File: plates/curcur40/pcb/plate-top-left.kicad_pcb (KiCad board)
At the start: 2 copper layers, 116.1 x 88.3 mm, 0 parts

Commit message: fix all
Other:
- board size 116.1 x 88.3 mm -> 125.1 x 92.6 mm
- rule pad_to_mask_clearance: 0.2 -> 0

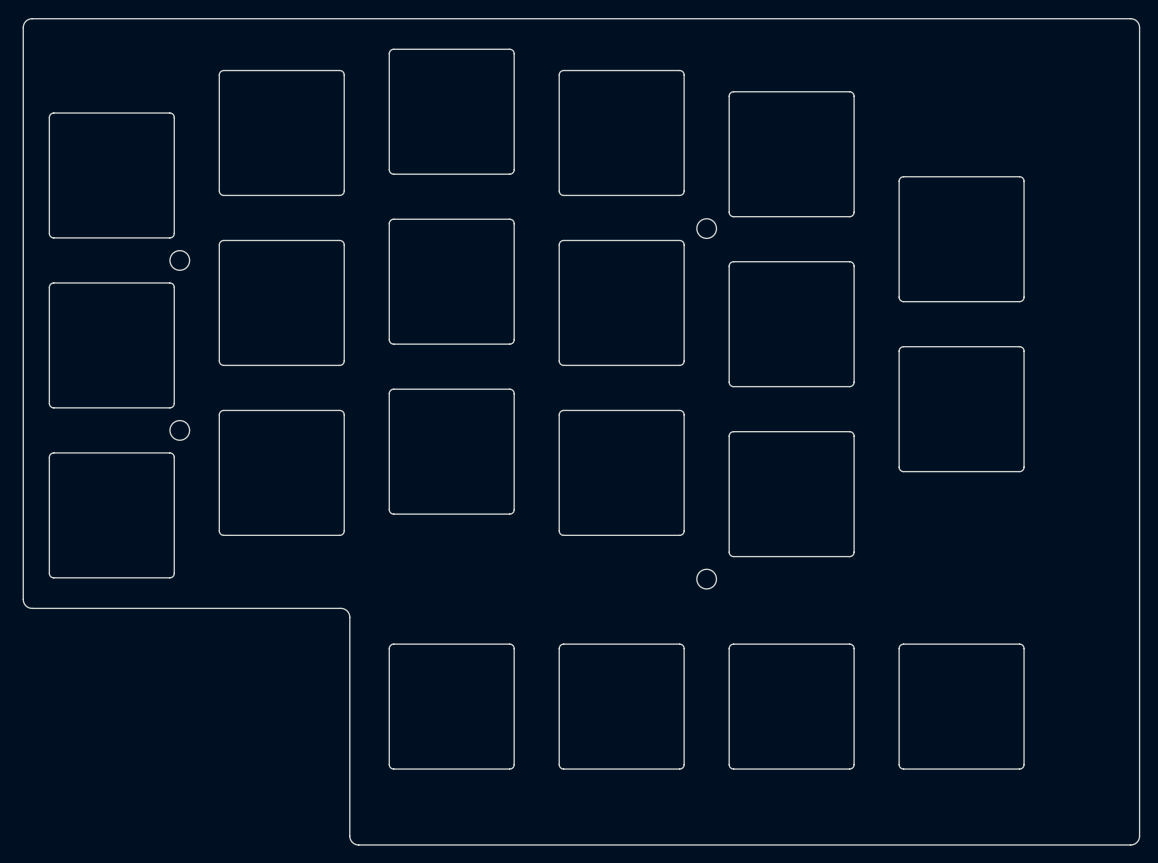
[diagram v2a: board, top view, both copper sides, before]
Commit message: Restore TRRS cutouts and relocate mounting holes to perimeter
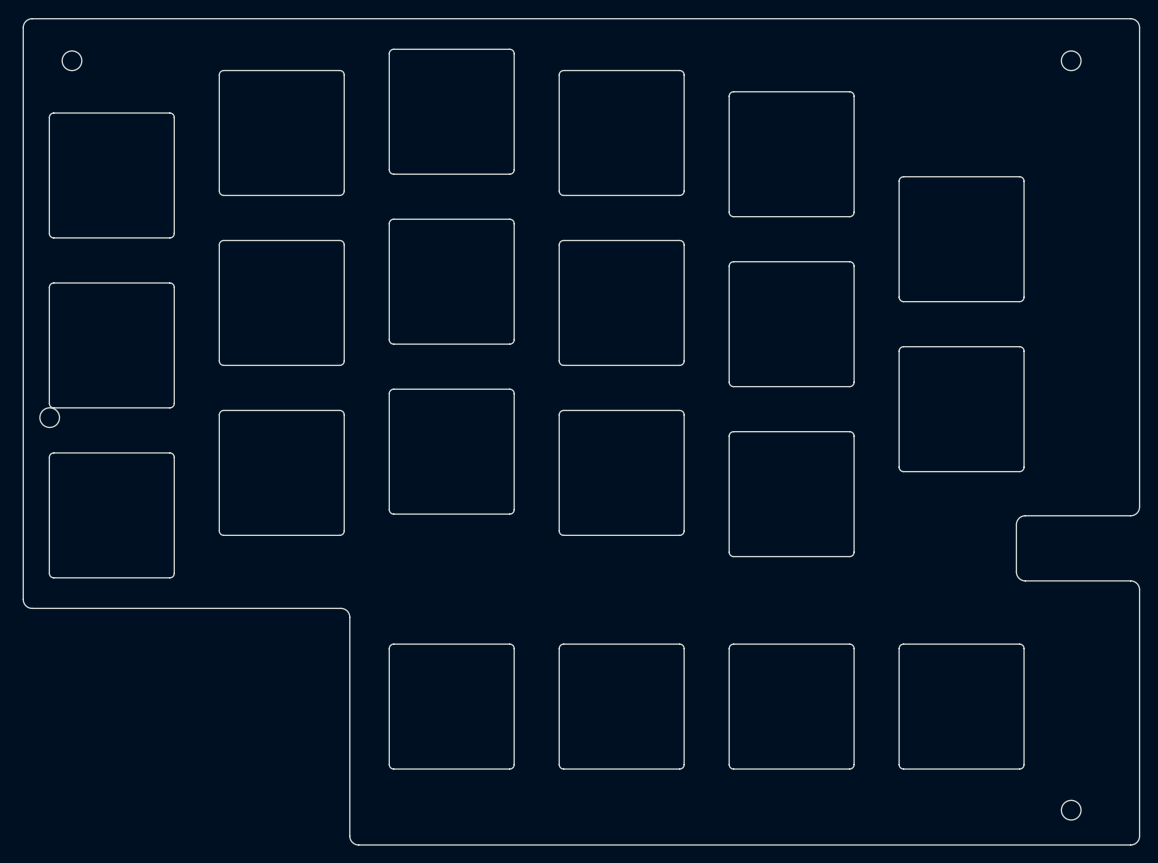
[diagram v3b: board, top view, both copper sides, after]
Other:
- outline, holes or cut-outs redrawn
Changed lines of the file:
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@@
+		(layer "Edge.Cuts")
+	)
+	(gr_circle
+		(center -116.5 20)
+		(end -115.4 20)
+		(stroke
+			(width 0.15)
+			(type default)
+		)
+		(fill no)
 		(layer "Edge.Cuts")
 	)
@@
 		(layer "Edge.Cuts")
 	)
+	(gr_circle
+		(center -114 -20)
+		(end -112.9 -20)
+		(stroke
+			(width 0.15)
+			(type default)
+		)
+		(fill no)
+		(layer "Edge.Cuts")
+	)
 	(gr_arc
 		(start -103.0375 -14.14375)
@@
 		(layer "Edge.Cuts")
 	)
-	(gr_circle
-		(center -101.9175 2.38125)
-		(end -100.8175 2.38125)
-		(stroke
-			(width 0.15)
-			(type default)
-		)
-		(fill no)
-		(layer "Edge.Cuts")
-	)
-	(gr_circle
-		(center -101.9175 21.43125)
-		(end -100.8175 21.43125)
-		(stroke
-			(width 0.15)
-			(type default)
-		)
-		(fill no)
-		(layer "Edge.Cuts")
-	)
 	(gr_arc
 		(start -97.4875 -18.40625)
@@
 		(layer "Edge.Cuts")
 	)
-	(gr_circle
-		(center -42.8625 -1.190625)
-		(end -41.762499 -1.190625)
-		(stroke
-			(width 0.15)
-			(type default)
-		)
-		(fill no)
-		(layer "Edge.Cuts")
-	)
-	(gr_circle
-		(center -42.8625 38.1)
-		(end -41.762499 38.1)
-		(stroke
-			(width 0.15)
-			(type default)
-		)
-		(fill no)
-		(layer "Edge.Cuts")
-	)
 	(gr_arc
 		(start -40.3375 -16.024999)
@@
 	)
 	(gr_arc
+		(start -8.1425 32)
+		(mid -7.849607 31.292893)
+		(end -7.1425 31)
+		(stroke
+			(width 0.15)
+			(type default)
+		)
+		(layer "Edge.Cuts")
+	)
+	(gr_line
+		(start -8.1425 37.3)
+		(end -8.1425 32)
+		(stroke
+			(width 0.15)
+			(type default)
+		)
+		(layer "Edge.Cuts")
+	)
+	(gr_arc
 		(start -7.7875 -7)
 		(mid -7.433947 -6.853553)
@@
 	)
 	(gr_line
+		(start -7.1425 31)
+		(end 4.6625 31)
+		(stroke
+			(width 0.15)
+			(type default)
+		)
+		(layer "Edge.Cuts")
+	)
+	(gr_arc
+		(start -7.1425 38.3)
+		(mid -7.849607 38.007107)
+		(end -8.1425 37.3)
+		(stroke
+			(width 0.15)
+			(type default)
+		)
+		(layer "Edge.Cuts")
+	)
+	(gr_circle
+		(center -2 -20)
+		(end -0.899999 -20)
+		(stroke
+			(width 0.15)
+			(type default)
+		)
+		(fill no)
+		(layer "Edge.Cuts")
+	)
+	(gr_circle
+		(center -2 64)
+		(end -0.899999 64)
+		(stroke
+			(width 0.15)
+			(type default)
+		)
+		(fill no)
+		(layer "Edge.Cuts")
+	)
+	(gr_line
 		(start 4.6625 -24.7125)
 		(end -118.4625 -24.7125)
@@
 		(layer "Edge.Cuts")
 	)
+	(gr_line
+		(start 4.6625 38.3)
+		(end -7.1425 38.3)
+		(stroke
+			(width 0.15)
+			(type default)
+		)
+		(layer "Edge.Cuts")
+	)
+	(gr_arc
+		(start 4.6625 38.3)
+		(mid 5.369607 38.592893)
+		(end 5.6625 39.3)
+		(stroke
+			(width 0.15)
+			(type default)
+		)
+		(layer "Edge.Cuts")
+	)
+	(gr_arc
+		(start 5.6625 30)
+		(mid 5.369607 30.707107)
+		(end 4.6625 31)
+		(stroke
+			(width 0.15)
+			(type default)
+		)
+		(layer "Edge.Cuts")
+	)
+	(gr_line
+		(start 5.6625 30)
+		(end 5.6625 -23.7125)
+		(stroke
+			(width 0.15)
+			(type default)
+		)
+		(layer "Edge.Cuts")
+	)
 	(gr_arc
 		(start 5.6625 66.9)
@@
 	(gr_line
 		(start 5.6625 66.9)
-		(end 5.6625 -23.7125)
-		(stroke
-			(width 0.15)
+		(end 5.6625 39.3)
+		(stroke
+			(width 0.15)

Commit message: fix trrs top plate
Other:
- outline, holes or cut-outs redrawn
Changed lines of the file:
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@@
-		(layer "Edge.Cuts")
-	)
-	(gr_circle
-		(center -116.5 20)
-		(end -115.4 20)
-		(stroke
-			(width 0.15)
-			(type default)
-		)
-		(fill no)
 		(layer "Edge.Cuts")
 	)
@@
 		(layer "Edge.Cuts")
 	)
-	(gr_circle
-		(center -114 -20)
-		(end -112.9 -20)
-		(stroke
-			(width 0.15)
-			(type default)
-		)
-		(fill no)
-		(layer "Edge.Cuts")
-	)
 	(gr_arc
 		(start -103.0375 -14.14375)
@@
 		(layer "Edge.Cuts")
 	)
+	(gr_circle
+		(center -100 -22.5)
+		(end -98.9 -22.5)
+		(stroke
+			(width 0.15)
+			(type default)
+		)
+		(fill no)
+		(layer "Edge.Cuts")
+	)
+	(gr_circle
+		(center -98 38)
+		(end -96.9 38)
+		(stroke
+			(width 0.15)
+			(type default)
+		)
+		(fill no)
+		(layer "Edge.Cuts")
+	)
 	(gr_arc
 		(start -97.4875 -18.40625)
@@
 		(layer "Edge.Cuts")
 	)
+	(gr_circle
+		(center -23.8125 -22.5)
+		(end -22.7125 -22.5)
+		(stroke
+			(width 0.15)
+			(type default)
+		)
+		(fill no)
+		(layer "Edge.Cuts")
+	)
+	(gr_circle
+		(center -23.8125 64)
+		(end -22.7125 64)
+		(stroke
+			(width 0.15)
+			(type default)
+		)
+		(fill no)
+		(layer "Edge.Cuts")
+	)
 	(gr_arc
 		(start -21.2875 -6.5)
@@
 	)
 	(gr_arc
-		(start -8.1425 32)
-		(mid -7.849607 31.292893)
-		(end -7.1425 31)
-		(stroke
-			(width 0.15)
-			(type default)
-		)
-		(layer "Edge.Cuts")
-	)
-	(gr_line
-		(start -8.1425 37.3)
-		(end -8.1425 32)
-		(stroke
-			(width 0.15)
-			(type default)
-		)
-		(layer "Edge.Cuts")
-	)
-	(gr_arc
 		(start -7.7875 -7)
 		(mid -7.433947 -6.853553)
@@
 	)
 	(gr_line
-		(start -7.1425 31)
-		(end 4.6625 31)
-		(stroke
-			(width 0.15)
-			(type default)
-		)
-		(layer "Edge.Cuts")
-	)
-	(gr_arc
-		(start -7.1425 38.3)
-		(mid -7.849607 38.007107)
-		(end -8.1425 37.3)
-		(stroke
-			(width 0.15)
-			(type default)
-		)
-		(layer "Edge.Cuts")
-	)
-	(gr_circle
-		(center -2 -20)
-		(end -0.899999 -20)
-		(stroke
-			(width 0.15)
-			(type default)
-		)
-		(fill no)
-		(layer "Edge.Cuts")
-	)
-	(gr_circle
-		(center -2 64)
-		(end -0.899999 64)
-		(stroke
-			(width 0.15)
-			(type default)
-		)
-		(fill no)
-		(layer "Edge.Cuts")
-	)
-	(gr_line
 		(start 4.6625 -24.7125)
 		(end -118.4625 -24.7125)
@@
 		(layer "Edge.Cuts")
 	)
-	(gr_line
-		(start 4.6625 38.3)
-		(end -7.1425 38.3)
-		(stroke
-			(width 0.15)
-			(type default)
-		)
-		(layer "Edge.Cuts")
-	)
-	(gr_arc
-		(start 4.6625 38.3)
-		(mid 5.369607 38.592893)
-		(end 5.6625 39.3)
-		(stroke
-			(width 0.15)
-			(type default)
-		)
-		(layer "Edge.Cuts")
-	)
-	(gr_arc
-		(start 5.6625 30)
-		(mid 5.369607 30.707107)
-		(end 4.6625 31)
-		(stroke
-			(width 0.15)
-			(type default)
-		)
-		(layer "Edge.Cuts")
-	)
-	(gr_line
-		(start 5.6625 30)
-		(end 5.6625 -23.7125)
-		(stroke
-			(width 0.15)
-			(type default)
-		)
-		(layer "Edge.Cuts")
-	)
 	(gr_arc
 		(start 5.6625 66.9)
@@
 	(gr_line
 		(start 5.6625 66.9)
-		(end 5.6625 39.3)
-		(stroke
-			(width 0.15)
+		(end 5.6625 -23.7125)
+		(stroke
+			(width 0.15)
